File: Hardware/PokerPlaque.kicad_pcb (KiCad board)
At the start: 2 copper layers, 54 x 43 mm, 7 parts, among them J1 Conn_01x05_Pin, J2 Conn_01x04_Pin, J3 Conn_01x08_Pin, J4 Conn_01x02_Pin, U2 ATtiny1616-M

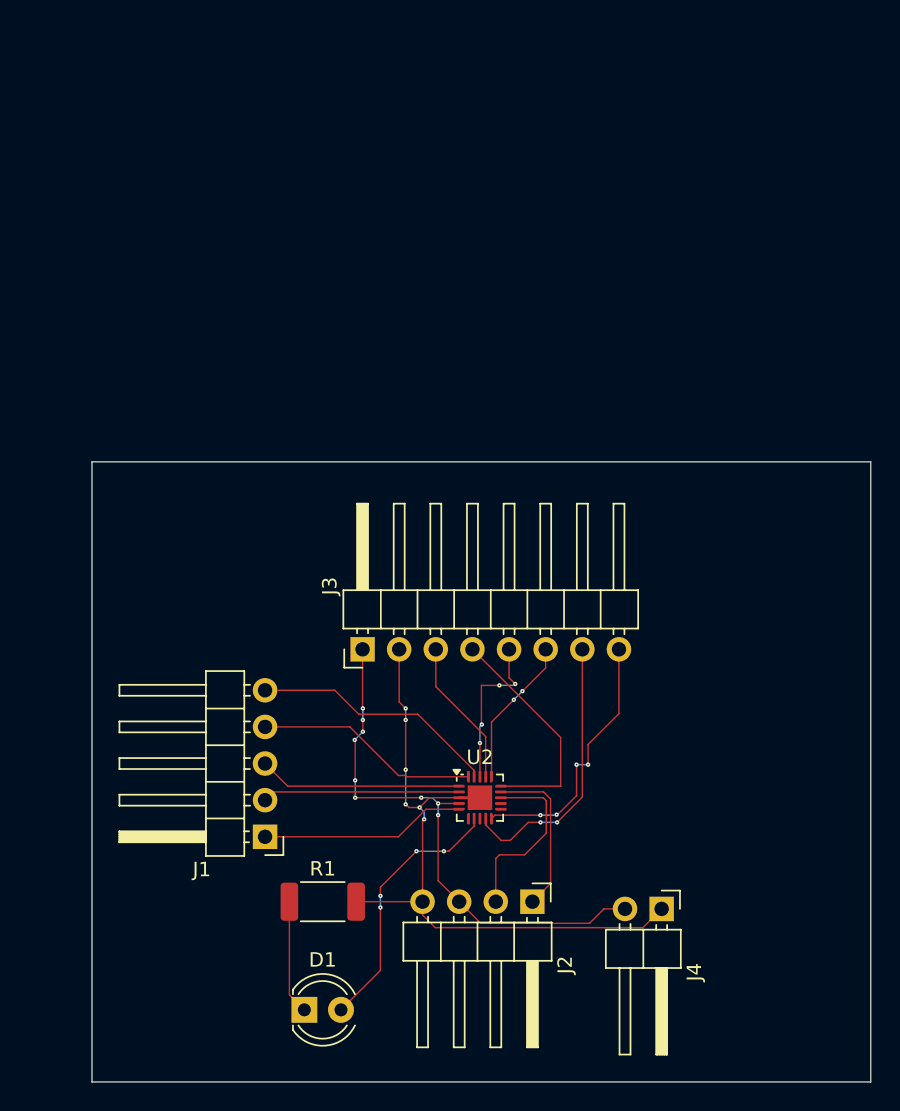
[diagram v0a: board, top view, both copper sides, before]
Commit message: Added labeling
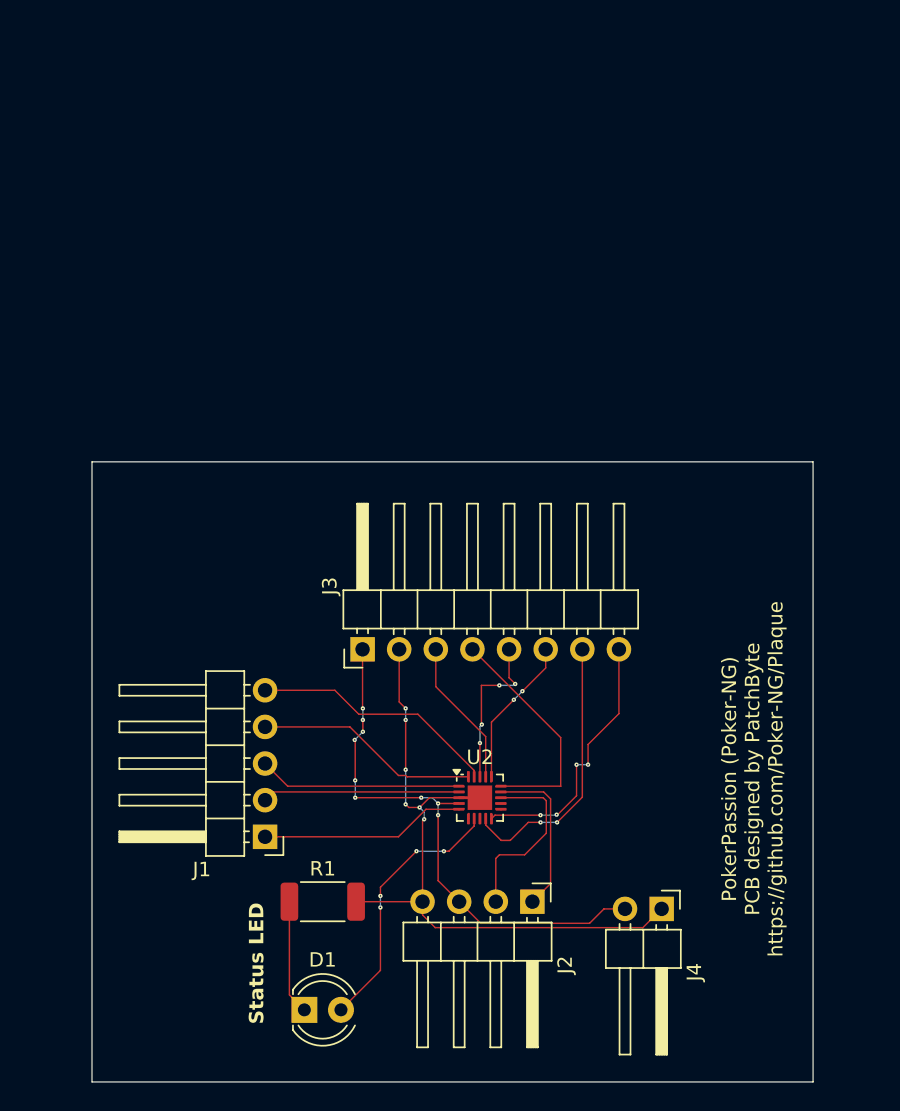
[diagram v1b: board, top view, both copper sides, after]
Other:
- board size 54 x 43 mm -> 50 x 43 mm
- board text added: "PokerPassion (Poker-NG) PCB designed by PatchByte https://github.com/Poker-NG/Plaque"
- board text added: "Status LED"
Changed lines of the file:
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@@
 		(tags "Through hole angled pin header THT 1x05 2.54mm single row")
 		(property "Reference" "J1"
-			(at 4.385 -2.27 360)
+			(at 4.385 -2.27 0)
 			(layer "F.SilkS")
 			(effects
@@
 		)
 		(property "Value" "Conn_01x05_Pin"
-			(at 4.385 12.43 360)
+			(at 4.385 12.43 0)
 			(layer "F.Fab")
 			(effects
@@
 		)
 		(fp_text user "${REFERENCE}"
-			(at 2.77 1.27 360)
+			(at 2.77 1.27 0)
 			(layer "F.Fab")
 			(effects
@@
 		)
 		(fp_text user "${REFERENCE}"
-			(at 2.77 3.81 360)
+			(at 2.77 3.81 0)
 			(layer "F.Fab")
 			(effects
@@
 		)
 		(fp_text user "${REFERENCE}"
-			(at 2.77 8.89 360)
+			(at 2.77 8.89 0)
 			(layer "F.Fab")
 			(effects
@@
 	(gr_rect
 		(start 26 50)
-		(end 80 93)
+		(end 76 93)
 		(stroke
 			(width 0.05)
@@
 		(layer "Edge.Cuts")
 	)
+	(gr_text "PokerPassion (Poker-NG)\nPCB designed by PatchByte\nhttps://github.com/Poker-NG/Plaque"
+		(at 74 72 90)
+		(layer "F.SilkS")
+		(effects
+			(font
+				(size 1 1)
+				(thickness 0.1)
+			)
+			(justify bottom)
+		)
+	)
+	(gr_text "Status LED"
+		(at 38 89 90)
+		(layer "F.SilkS")
+		(effects
+			(font
+				(size 1 1)
+				(thickness 0.2)
+				(bold yes)
+			)
+			(justify left bottom)
+		)
+	)
 	(segment

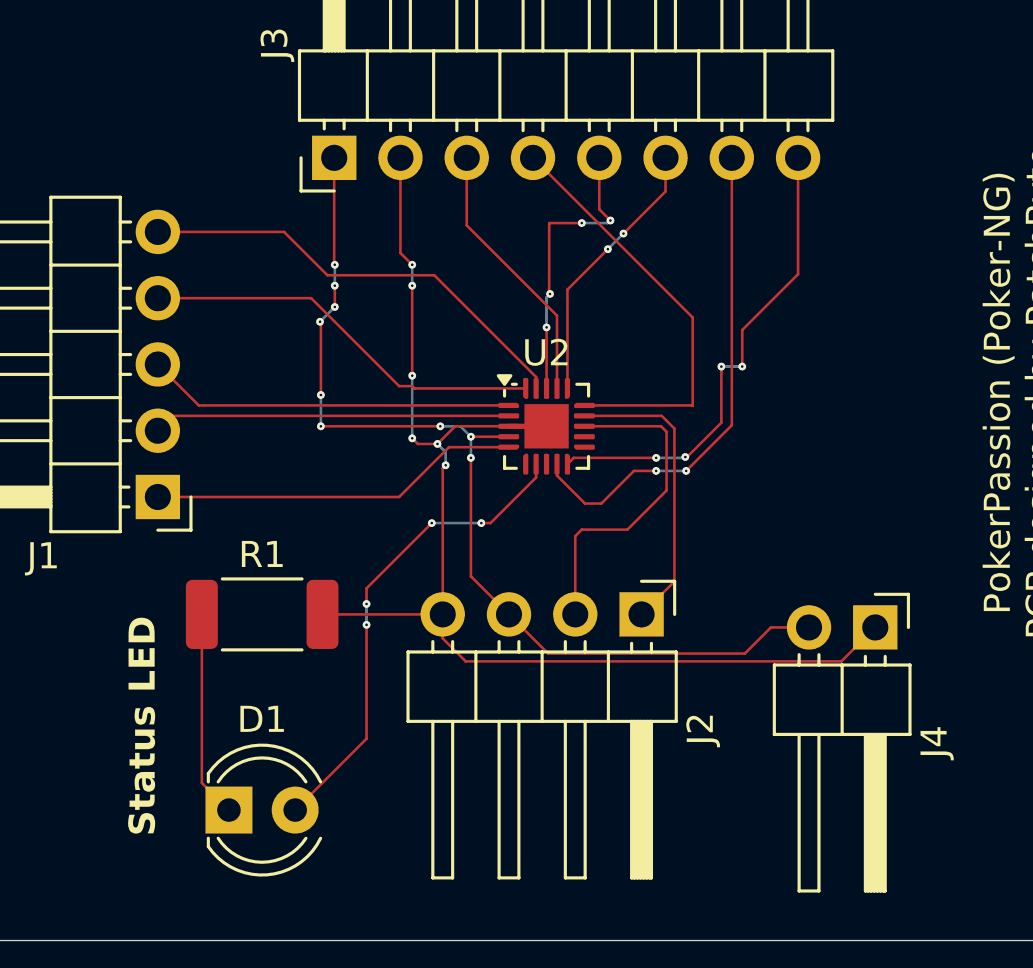
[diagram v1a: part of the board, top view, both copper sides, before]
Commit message: Increased Via Size
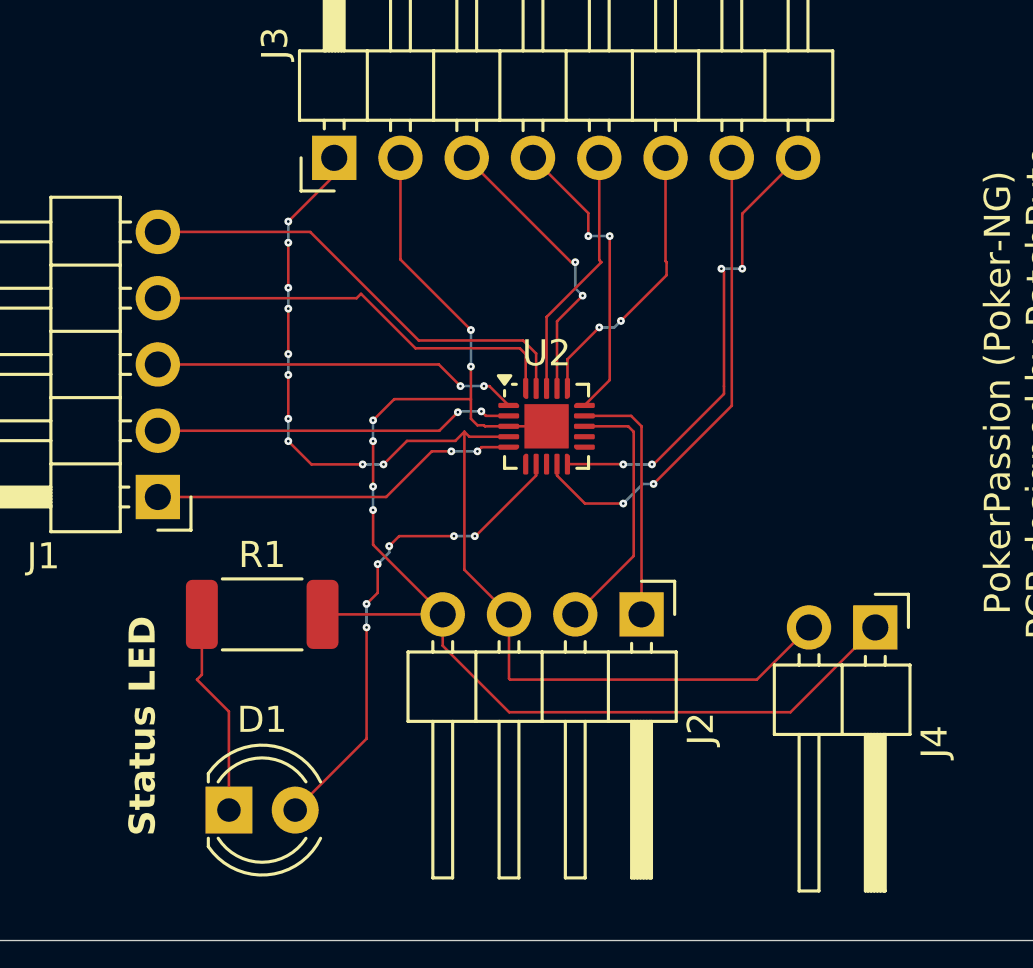
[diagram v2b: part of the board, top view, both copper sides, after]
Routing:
- net VCC: track 37.9 -> 43.5 mm, vias 9 -> 10
- net GND: track 46.2 -> 51.6 mm
- net Sck1: track 16.2 -> 11.6 mm, vias 0 -> 2
- net SDA: track 12.7 -> 9.90 mm
- net SCL: track 11.3 -> 9.57 mm
- net Ss1: track 11.4 -> 9.74 mm, vias 4 -> 0
- net /Mosi0: track 15.5 -> 16.4 mm
- net Mosi1: track 10.3 -> 11.2 mm, vias 0 -> 2
- net /Reset0: track 17.2 -> 17.8 mm
- net Led0: track 18.4 -> 18.8 mm, vias 4 -> 6
- net /Sck0: track 13.7 -> 13.8 mm, vias 0 -> 2
- net /Ss0: vias 0 -> 2
- net /Miso0: vias 0 -> 2

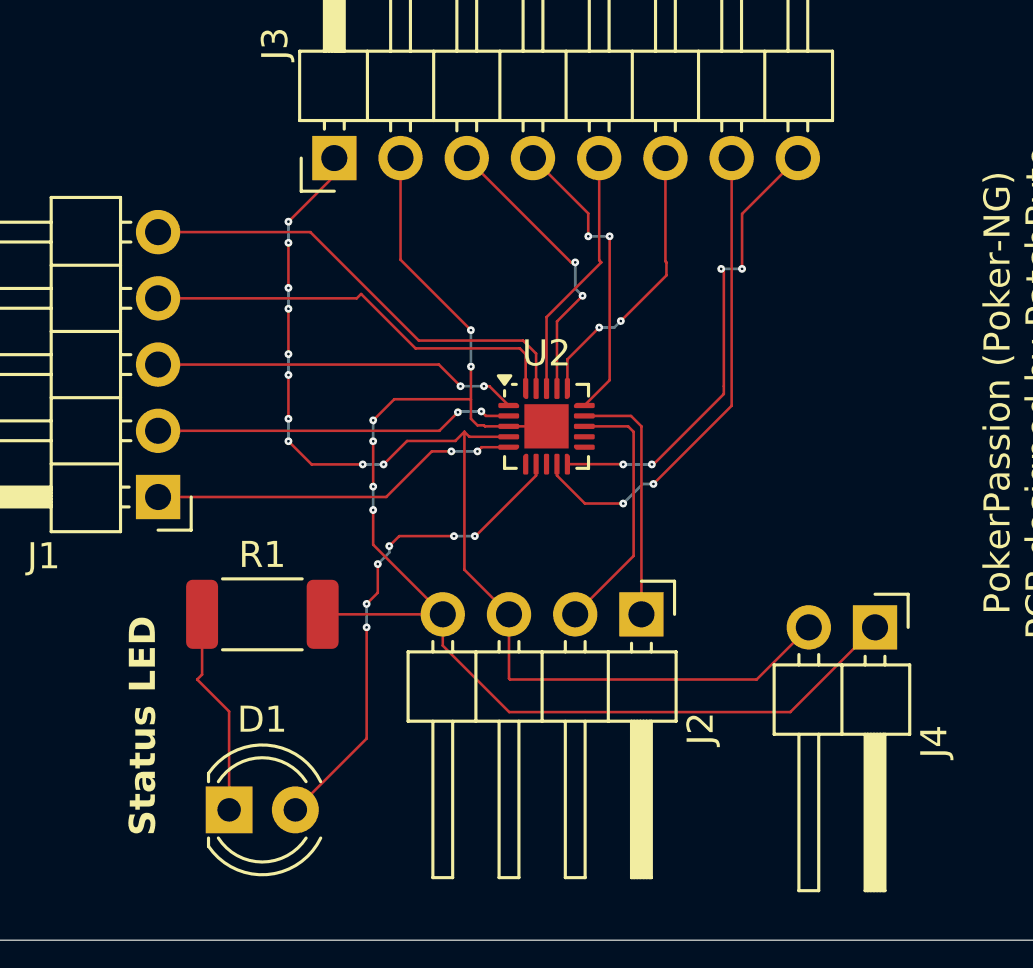
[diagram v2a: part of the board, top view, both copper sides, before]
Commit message: Reworked tracks and vias
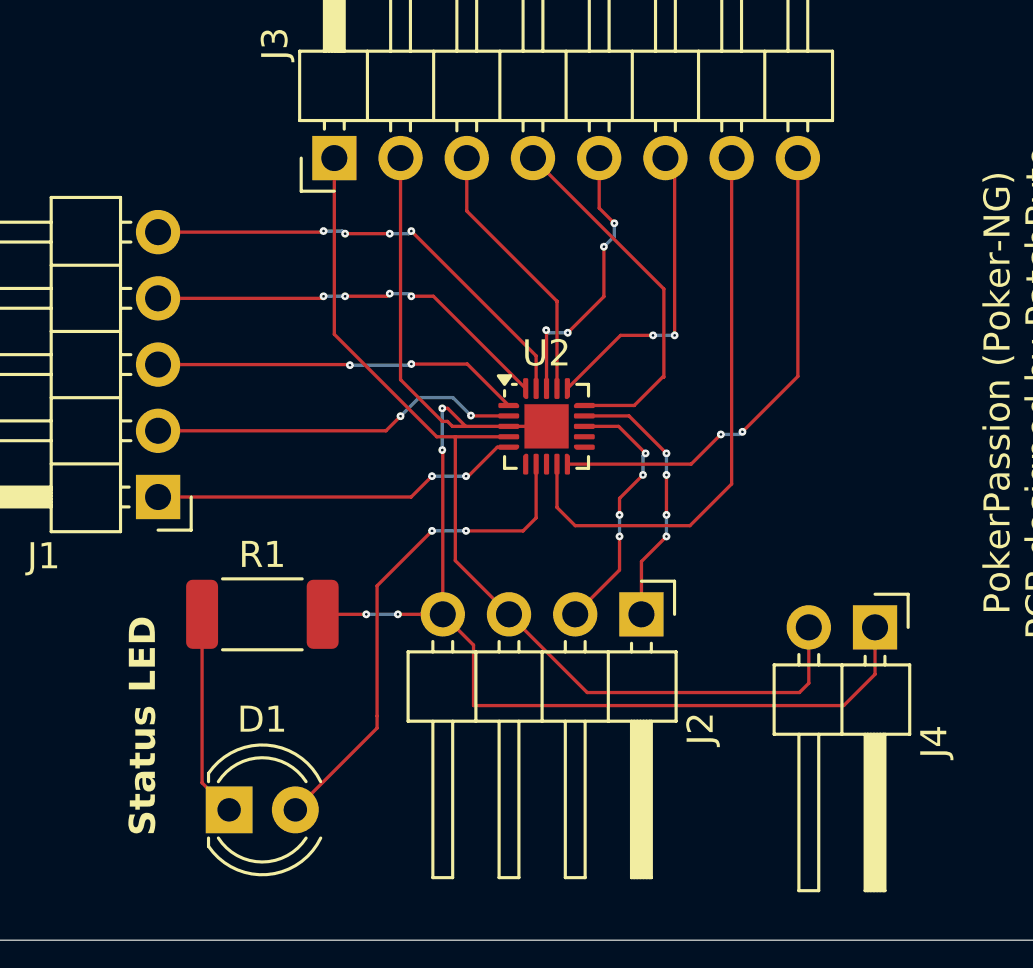
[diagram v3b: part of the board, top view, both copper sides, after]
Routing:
- net VCC: track 43.5 -> 37.8 mm, vias 10 -> 0
- net DspRst: track 18.6 -> 21.8 mm, vias 2 -> 0
- net Sck1: track 11.6 -> 14.0 mm, vias 2 -> 0
- net GND: track 51.6 -> 50.2 mm, vias 6 -> 4
- net Miso1: track 10.8 -> 11.9 mm
- net Ss1: track 9.74 -> 10.8 mm, vias 0 -> 4
- net Mosi1: track 11.2 -> 10.3 mm, vias 2 -> 0
- net /Mosi0: track 16.4 -> 15.7 mm, vias 0 -> 4
- net SCL: track 9.57 -> 10.3 mm, vias 0 -> 4
- net DspBusy: track 17.9 -> 18.6 mm, vias 4 -> 2
- net Led0: track 18.8 -> 19.1 mm, vias 6 -> 2
- net SDA: track 9.90 -> 10.1 mm, vias 0 -> 4
- net /Reset0: vias 0 -> 4

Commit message: Replaced micro vias with normal vias
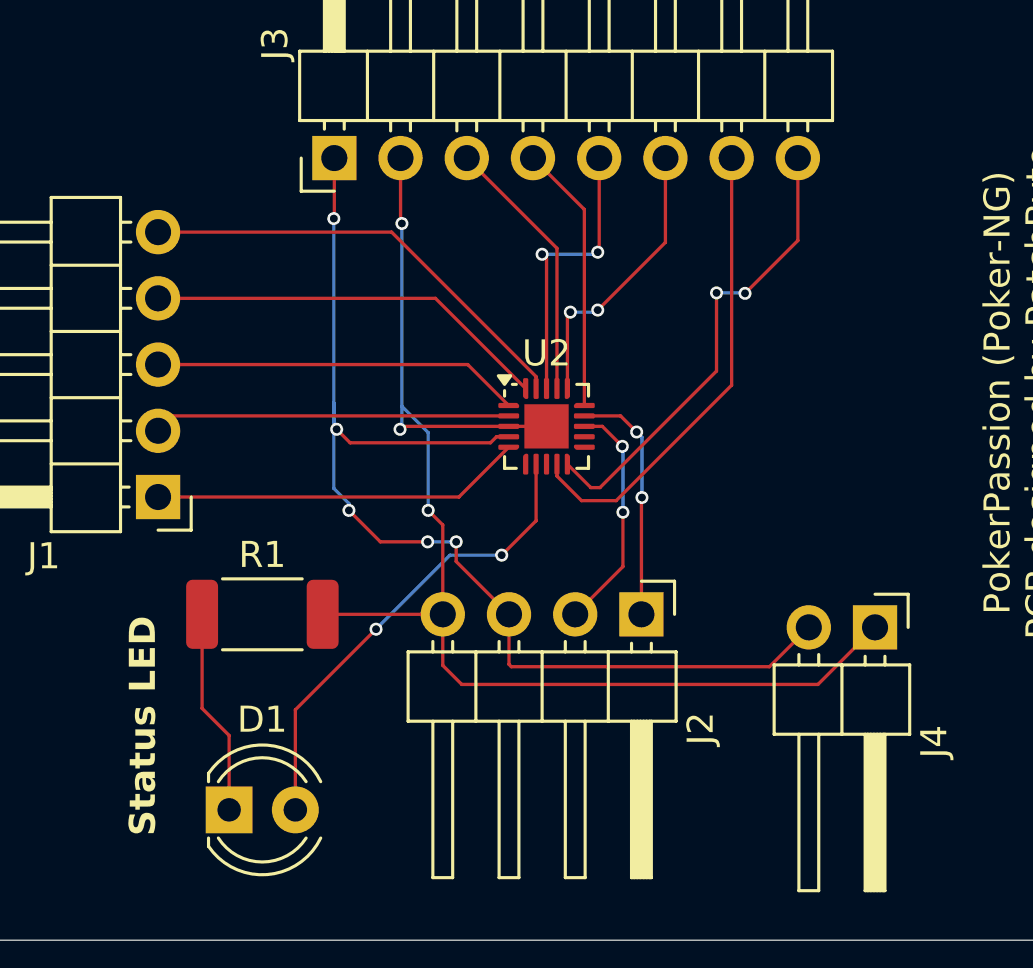
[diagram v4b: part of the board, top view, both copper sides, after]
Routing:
- net VCC: track 37.8 -> 44.0 mm, vias 0 -> 5
- net DspRst: track 21.8 -> 18.1 mm
- net Sck1: track 14.0 -> 10.3 mm
- net GND: track 50.2 -> 49.1 mm, vias 4 -> 3
- net SDA: track 10.1 -> 8.99 mm, vias 4 -> 2
- net SCL: track 10.3 -> 9.35 mm, vias 4 -> 2
- net Miso1: track 11.9 -> 11.0 mm
- net Led0: track 19.1 -> 18.2 mm
- net /Sck0: track 14.3 -> 13.7 mm, vias 2 -> 0
- net /Reset0: track 17.8 -> 17.3 mm, vias 4 -> 0
- net DspBusy: track 18.6 -> 18.1 mm
- net Ss1: track 10.8 -> 11.0 mm, vias 4 -> 2
- net /Mosi0: track 15.7 -> 15.5 mm, vias 4 -> 0
- net /Miso0: vias 2 -> 0
- net /Ss0: vias 2 -> 0
